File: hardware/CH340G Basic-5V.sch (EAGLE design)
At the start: 24 parts, among them J1 microB, U1 AP2112-3.3V, U2 CH340G, Y2 12MHz

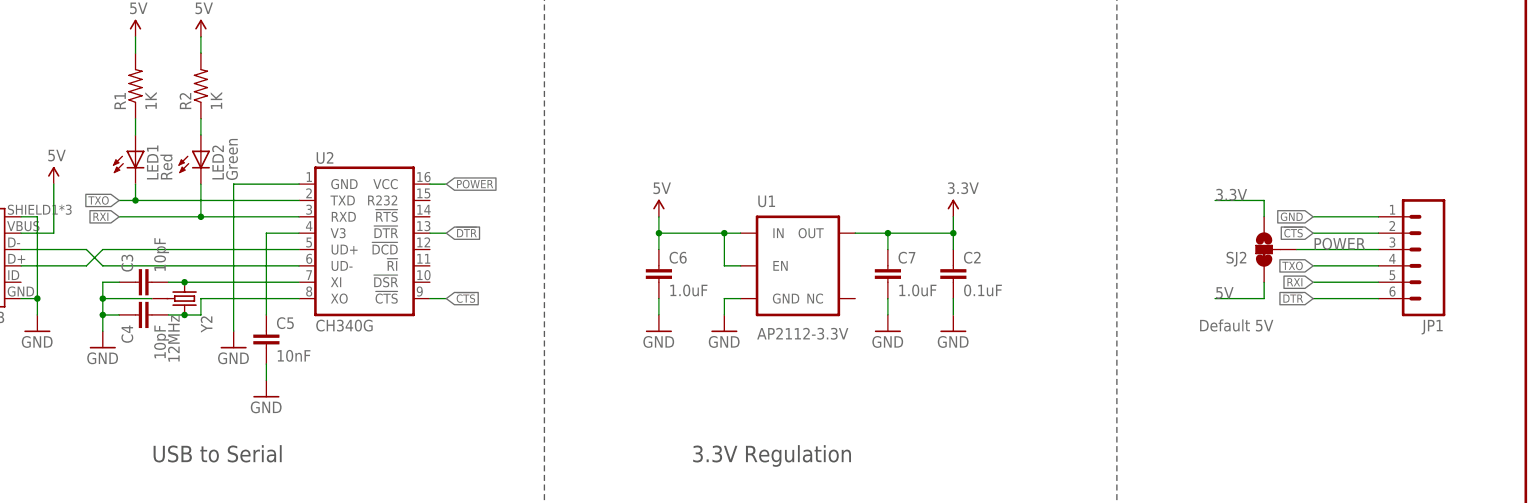
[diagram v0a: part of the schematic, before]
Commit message: Added TP to 3.3V. Passes checklist.
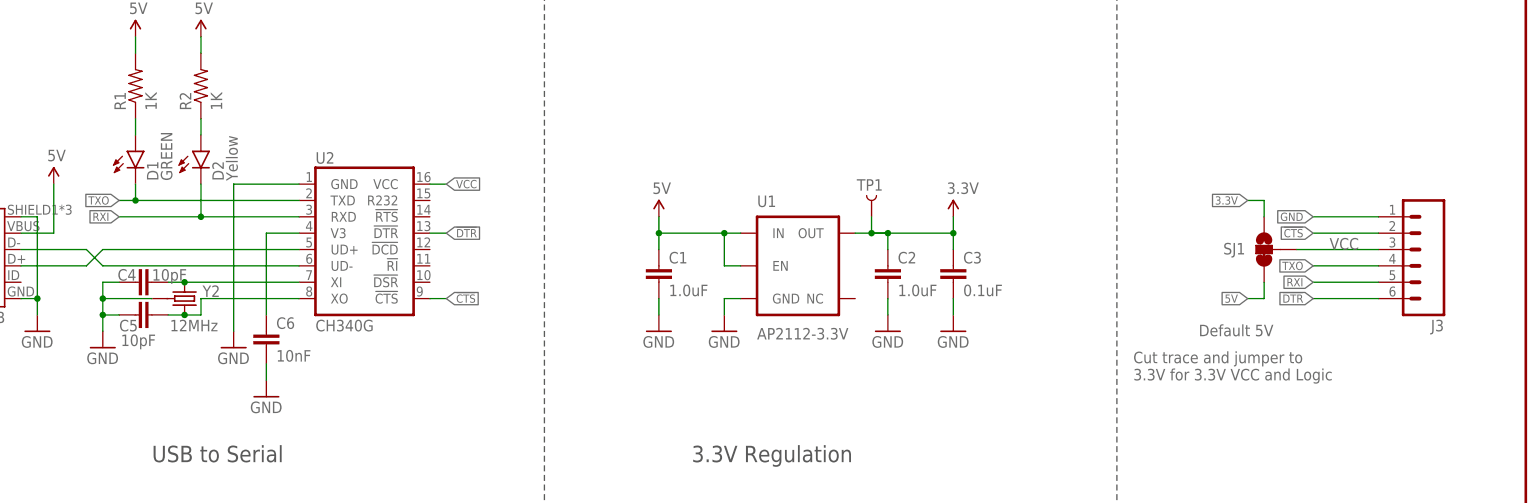
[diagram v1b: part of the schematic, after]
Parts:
- removed C7: 1.0uF, SparkFun-Capacitors:1.0UF-16V-10%(0603)
- removed JP1: (no value), SparkFun:M06SMD-FEMALE-V2
- removed LED1: Red, SparkFun:LED0603
- removed LED2: Green, SparkFun:LED0603
- added C1: 1.0uF, SparkFun-Capacitors:1.0UF-16V-10%(0603)
- added D1: GREEN, SparkFun-LED:LED-GREEN0603
- added D2: Yellow, SparkFun-LED:LED-YELLOW0603
- added J3: (no value), SparkFun-Connectors:M06SMD-FEMALE-V2
- added TP1: 3.3V TP, SparkFun-Passives:TEST-POINT3
- C2: value 0.1uF -> 1.0uF; device SparkFun:CAP0603-CAP -> SparkFun-Capacitors:1.0UF-16V-10%(0603)
- C3: value 10pF -> 0.1uF; device SparkFun-Capacitors:10PF-50V-5%(0603) -> SparkFun-Capacitors:0.1UF-25V(+80/-20%)(0603)
- C5: value 10nF -> 10pF; device SparkFun-Capacitors:10NF/10000PF-50V-10%(0603) -> SparkFun-Capacitors:10PF-50V-5%(0603)
- C6: value 1.0uF -> 10nF; device SparkFun-Capacitors:1.0UF-16V-10%(0603) -> SparkFun-Capacitors:10NF/10000PF-50V-10%(0603)
- R1, R2: device SparkFun:RESISTOR0603-RES -> SparkFun-Resistors:1KOHM-1/10W-1%(0603)
- renumbered SJ2 to SJ1
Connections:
- removed net POWER: JP1.3, SJ1.2, U2.VCC
- new net VCC: J3.3, SJ1.2, U2.VCC
- net !CTS: now also J3.2; no longer JP1.2
- net !DTR: now also J3.6; no longer JP1.6
- net 3.3V: now also C3.1, TP1.1; no longer C7.1
- net 5V: now also C1.1; no longer C6.1
- net GND: now also C1.2, C3.2, C5.1, J3.1; no longer C3.1, C5.2, C7.2, JP1.1
- net N$1: now also D1.A; no longer LED1.A
- net N$2: now also D2.A; no longer LED2.A
- net N$3: now also C5.2; no longer C4.2
- net N$4: now also C4.2; no longer C3.2
- net RXI: now also D2.C, J3.5; no longer JP1.5, LED2.C
- net TXO: now also D1.C, J3.4; no longer JP1.4, LED1.C
- net V3: now also C6.1; no longer C5.1
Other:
- note added: "Cut trace and jumper to 3.3V for 3.3V VCC and Logic"
- moved on the sheet: C2, C3, C4, C5, C6
